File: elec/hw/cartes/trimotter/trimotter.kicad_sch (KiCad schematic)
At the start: 74 parts, among them J2 22053051, J3 2-1445055-2, J4 2-1445055-3, J5 3-794630-6, J6 3-794630-4, Q1 2N7002, U1 DRV8243HQDGQRQ1, U2 SN74LVC2T45DCU, U4 PCA9535PW

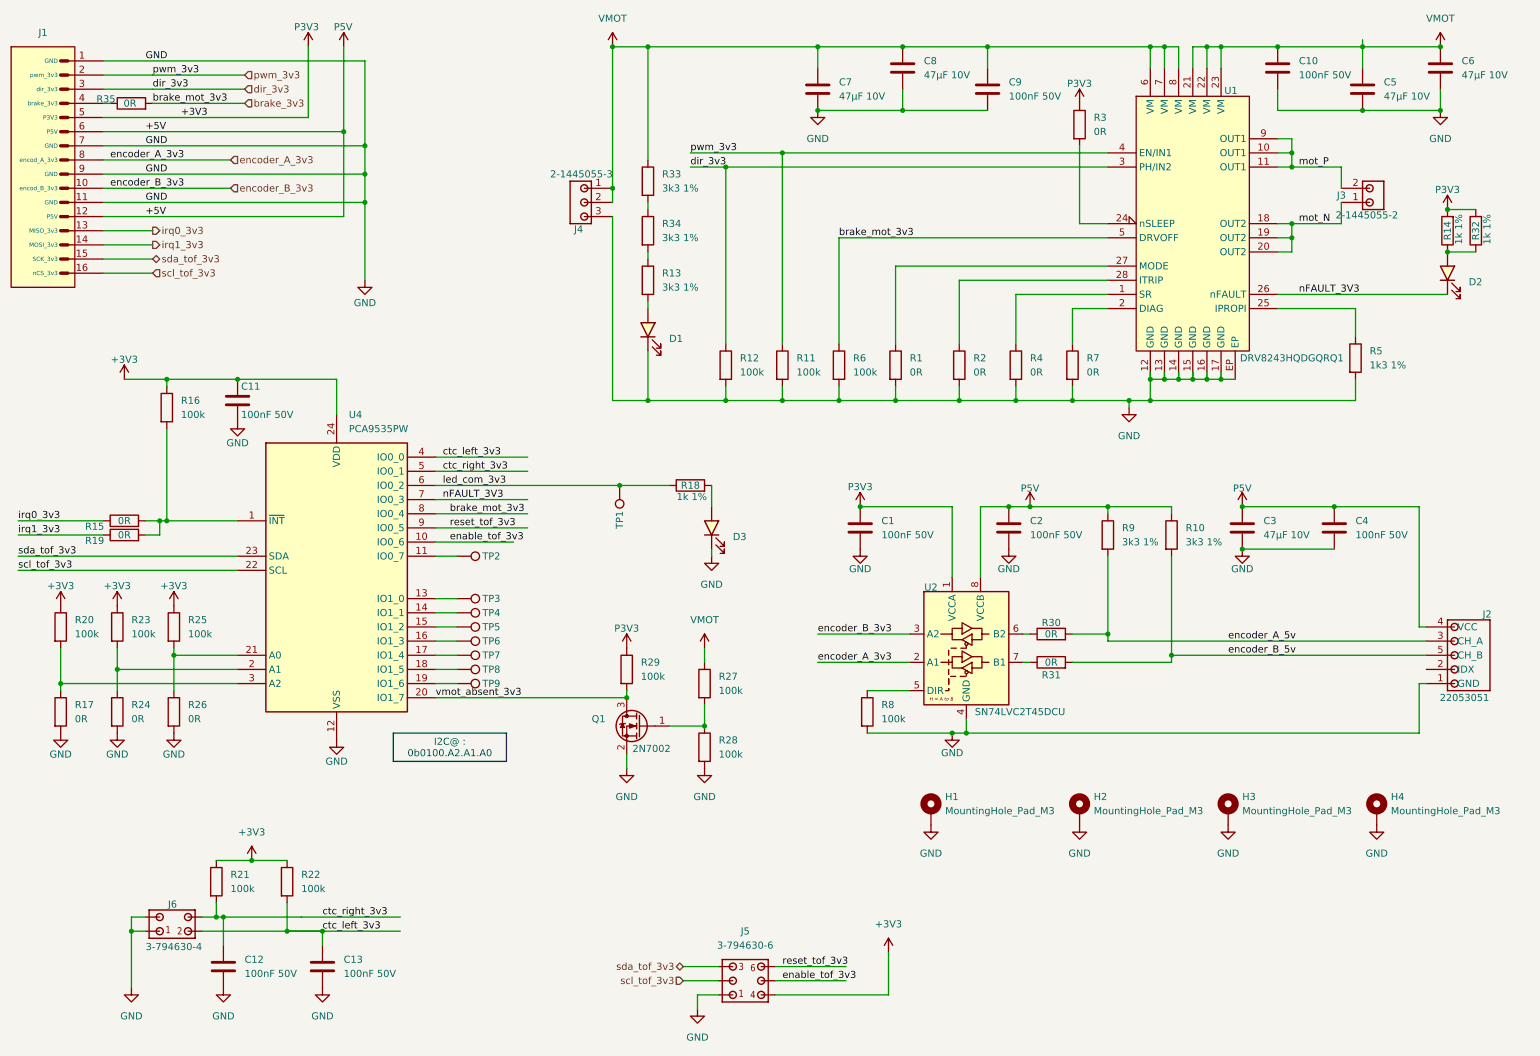
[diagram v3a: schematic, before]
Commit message: trimotter : schematic modified to match hack after board debug
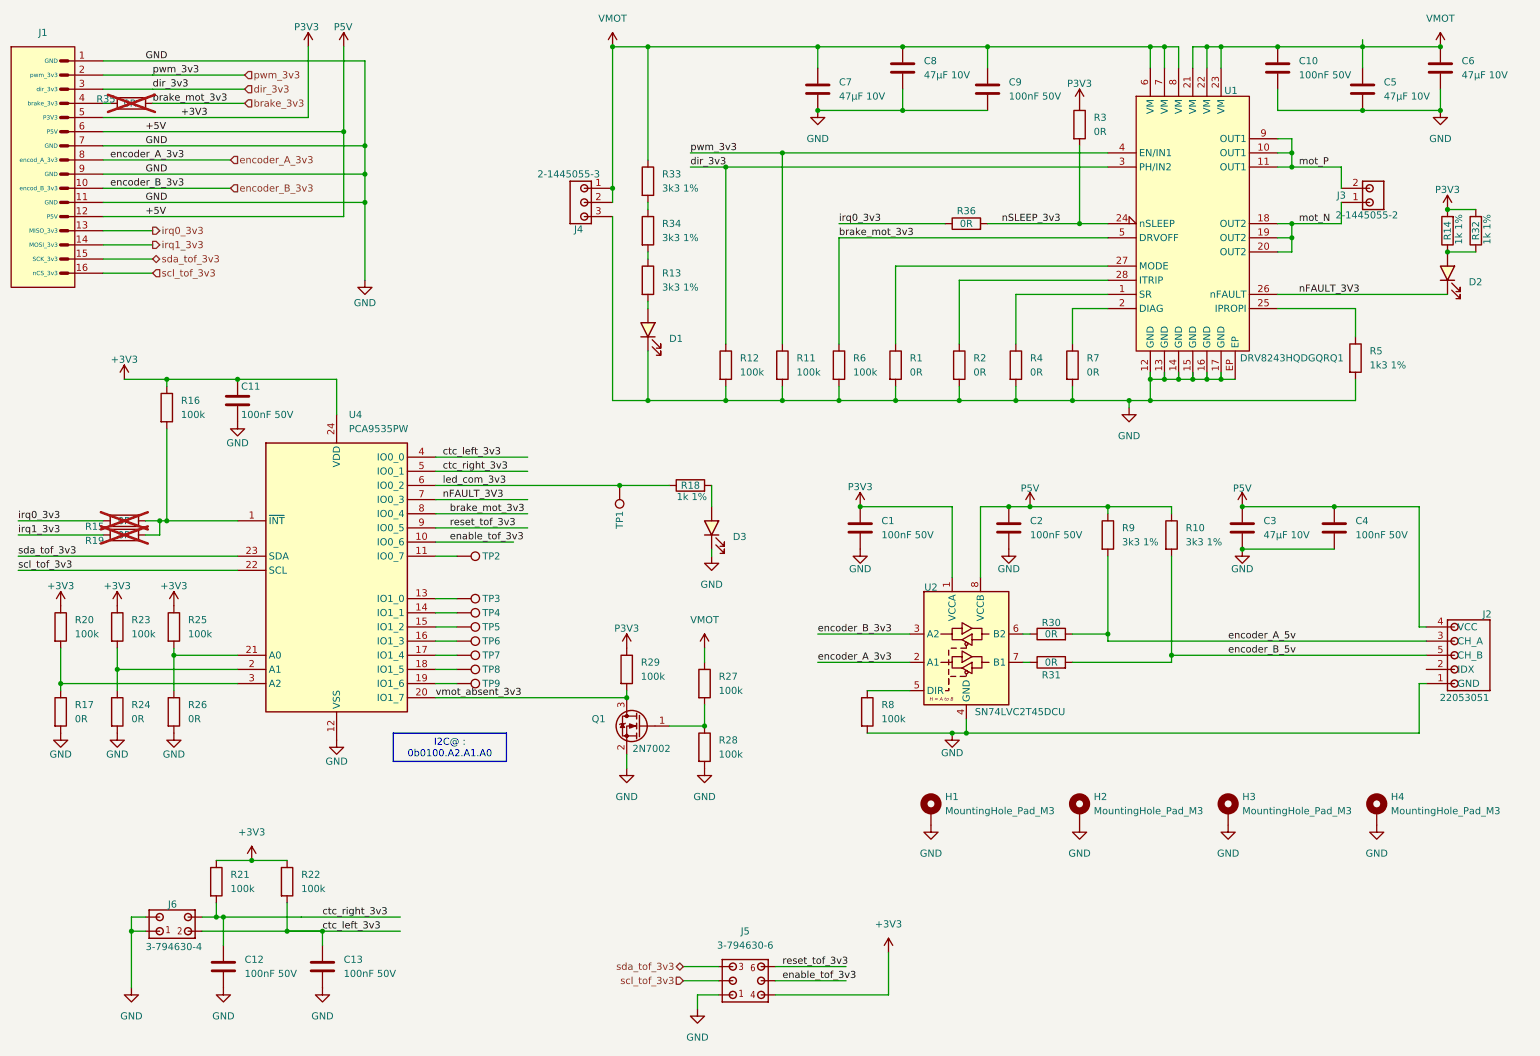
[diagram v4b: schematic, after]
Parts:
- added R36: 0R, cocotter_resistor:r0603_reflow, symbol cocotter_resistors:R_0R_0603
- R15, R19, R35: now not fitted
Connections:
- net irq0_3v3: now also R36.1
- net nSLEEP_3v3: now reaches R3.2, U1.24 (nSLEEP)
- net nSLEEP_3v3: now also R36.2
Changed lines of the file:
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@@
 (kicad_sch
-	(version 20231120)
+	(version 20250114)
 	(generator "eeschema")
-	(generator_version "8.0")
+	(generator_version "9.0")
 	(paper "A4")
+	(text_box "I2C@ : 0b0100.A2.A1.A0"
+		(exclude_from_sim no)
+		(at 83.82 142.24 0)
+		(size 20.32 5.08)
+		(margins 0.9525 0.9525 0.9525 0.9525)
+		(stroke
+			(width 0)
+			(type default)
+		)
+		(fill
+			(type color)
+			(color 0 194 0 1)
+		)
+		(effects
+			(font
+				(size 1.27 1.27)
+			)
+		)
+	)
 	(junction
 		(at 245.11 50.8)
@@
 	)
 	(junction
+		(at 207.01 50.8)
+		(diameter 0)
+		(color 0 0 0 0)
+	)
+	(junction
 		(at 236.22 101.6)
 		(diameter 0)
@@
 	(wire
 		(pts
+			(xy 163.83 50.8) (xy 182.88 50.8)
+		)
+		(stroke
+			(width 0)
+			(type default)
+		)
+	)
+	(wire
+		(pts
 			(xy 160.02 19.05) (xy 175.26 19.05)
 		)
@@
 	(wire
 		(pts
-			(xy 207.01 36.83) (xy 207.01 50.8)
-		)
-		(stroke
-			(width 0)
-			(type default)
-		)
-	)
-	(wire
-		(pts
 			(xy 195.58 82.55) (xy 205.74 82.55)
 		)
@@
 	(wire
 		(pts
+			(xy 190.5 50.8) (xy 207.01 50.8)
+		)
+		(stroke
+			(width 0)
+			(type default)
+		)
+	)
+	(wire
+		(pts
 			(xy 123.19 44.45) (xy 123.19 46.99)
 		)
@@
 	(wire
 		(pts
+			(xy 207.01 36.83) (xy 207.01 50.8)
+		)
+		(stroke
+			(width 0)
+			(type default)
+		)
+	)
+	(wire
+		(pts
 			(xy 224.79 19.05) (xy 224.79 22.86)
 		)
@@
 		)
 	)
-	(text_box "I2C@ : 0b0100.A2.A1.A0"
-		(exclude_from_sim no)
-		(at 83.82 142.24 0)
-		(size 20.32 5.08)
-		(stroke
-			(width 0)
-			(type default)
-		)
-		(fill
-			(type color)
-			(color 0 194 0 1)
-		)
-		(effects
-			(font
-				(size 1.27 1.27)
-			)
-		)
-	)
 	(label "sda_tof_3v3"
 		(at 16.51 110.49 0)
@@
 		)
 	)
+	(label "irq0_3v3"
+		(at 163.83 50.8 0)
+		(effects
+			(font
+				(size 1.27 1.27)
+			)
+			(justify left bottom)
+		)
+	)
 	(label "encoder_A_5v"
 		(at 233.68 125.73 0)
@@
 		)
 	)
+	(label "nSLEEP_3v3"
+		(at 193.04 50.8 0)
+		(effects
+			(font
+				(size 1.27 1.27)
+			)
+			(justify left bottom)
+		)
+	)
 	(label "GND"
 		(at 39.37 41.91 0)
@@
 		(in_bom yes)
 		(on_board yes)
-		(dnp no)
+		(dnp yes)
 		(property "Reference" "R15"
 			(at 30.226 105.156 90)
@@
 		(in_bom yes)
 		(on_board yes)
-		(dnp no)
+		(dnp yes)
 		(property "Reference" "R35"
 			(at 32.258 28.448 90)
@@
 	)
 	(symbol
+		(lib_id "cocotter_resistors:R_0R_0603")
+		(at 186.69 50.8 90)
+		(unit 1)
+		(exclude_from_sim no)
+		(in_bom yes)
+		(on_board yes)
+		(dnp no)
+		(property "Reference" "R36"
+			(at 186.69 48.514 90)
+			(effects
+				(font
+					(size 1.27 1.27)
+				)
+			)
+		)
+		(property "Value" "0R"
+			(at 186.69 50.8 90)
+			(effects
+				(font
+					(size 1.27 1.27)
+				)
+			)
+		)
+		(property "Footprint" "cocotter_resistor:r0603_reflow"
+			(at 186.69 52.578 90)
+			(effects
+				(font
+					(size 1.27 1.27)
+				)
+				(hide yes)
+			)
+		)
+		(property "Datasheet" "~"
+			(at 186.69 50.8 0)
+			(effects
+				(font
+					(size 1.27 1.27)
+				)
+				(hide yes)
+			)
+		)
+		(property "Description" "Resistor"
+			(at 186.69 50.8 0)
+			(effects
+				(font
+					(size 1.27 1.27)
+				)
+				(hide yes)
+			)
+		)
+		(property "Specification" "0R 0603 20mOhms max 100mW"
+			(at 186.69 50.8 0)
+			(effects
+				(font
+					(size 1.27 1.27)
+				)
+				(hide yes)
+			)
+		)
+		(property "mouser" ""
+			(at 186.69 50.8 0)
+			(effects
+				(font
+					(size 1.27 1.27)
+				)
+				(hide yes)
+			)
+		)
+		(property "JLCPCB Part #" "C431718"
+			(at 186.69 50.8 0)
+			(effects
+				(font
+					(size 1.27 1.27)
+				)
+				(hide yes)
+			)
+		)
+		(pin "2"
+		)
+		(pin "1"
+		)
+		(instances
+			(project "trimotter"
+				(path "/a60dda8c-8f9a-4dc6-a26e-76becdf78bf7"
+					(reference "R36")
+					(unit 1)
+				)
+			)
+		)
+	)
+	(symbol
 		(lib_id "cocotter_resistors:R_100k_0603_1%")
 		(at 125.73 130.81 0)
@@
 		(in_bom yes)
 		(on_board yes)
-		(dnp no)
+		(dnp yes)
 		(property "Reference" "R19"
 			(at 30.226 107.696 90)
@@
 		)
 		(property "Value" "2-1445055-3"
-			(at 117.602 41.91 0)
+			(at 115.316 41.91 0)
 			(effects
 				(font
@@
 		)
 	)
+	(embedded_fonts no)
 )
